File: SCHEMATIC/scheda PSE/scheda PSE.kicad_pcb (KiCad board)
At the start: 2 copper layers, 102.4 x 77.4 mm, 148 parts, among them J1 Conn_01x03, J2 Vin, J3 USB_B_Mini, J4 Vout 5V, J5 I2C_3V3, J6 UART0_3V3, Q1 IRLML0060TRPBF, Q2 PDTC114YT, Q3 IRLML9301, SW1 RESET_SW, SW2 PROG_SW, SW3 SW_U, SW4 SW_L, SW5 SW_R, SW6 SW_D, SW7 Power_button, U1 RP2040, U2 W25Q16JVUSSQ, U3 AT24C256, U4 oled_0.96"_128x64px, U5 TPS563201, U6 XC6705A331MR-G, U7 SAM-M8Q, U8 MMA8451Q, U9 TC1047A, Y1 12MHz

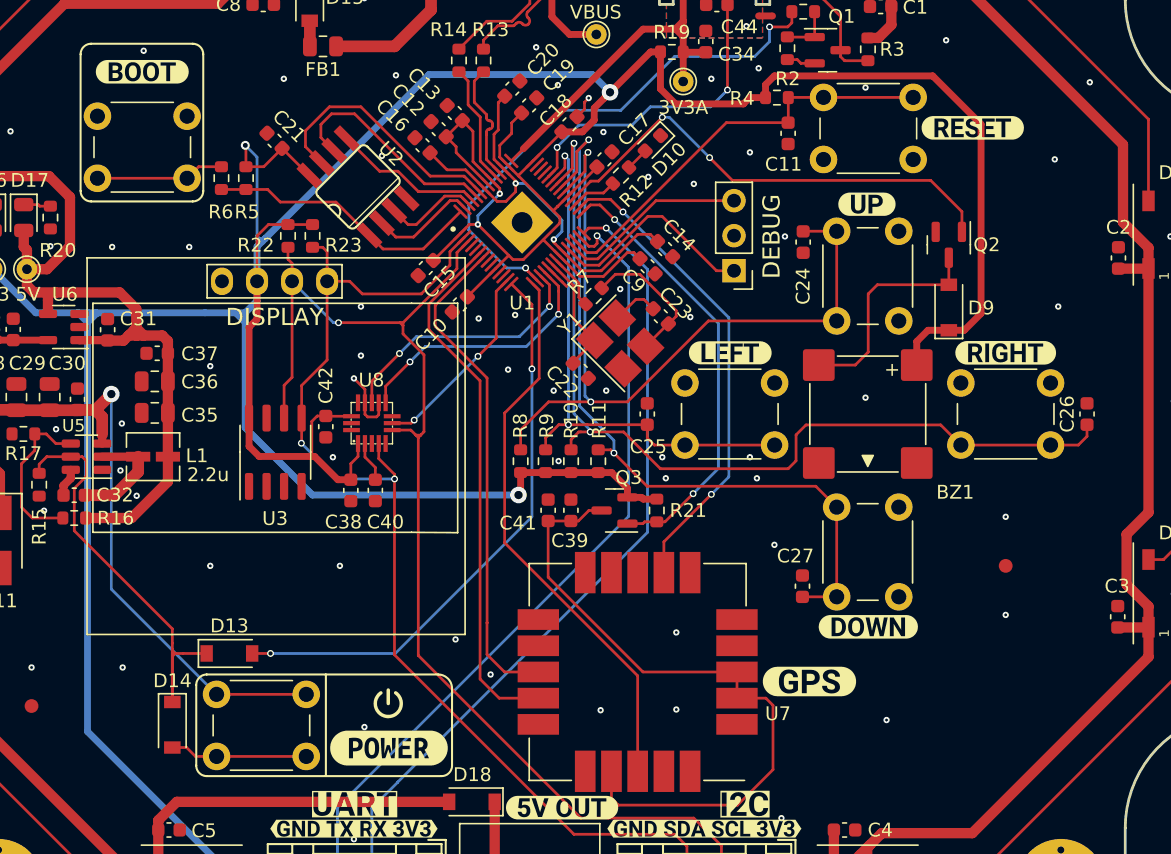
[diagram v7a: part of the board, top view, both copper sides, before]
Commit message: cambiati i pulsanti in smd
se servono gli altri pulsanti usare la versione precedente
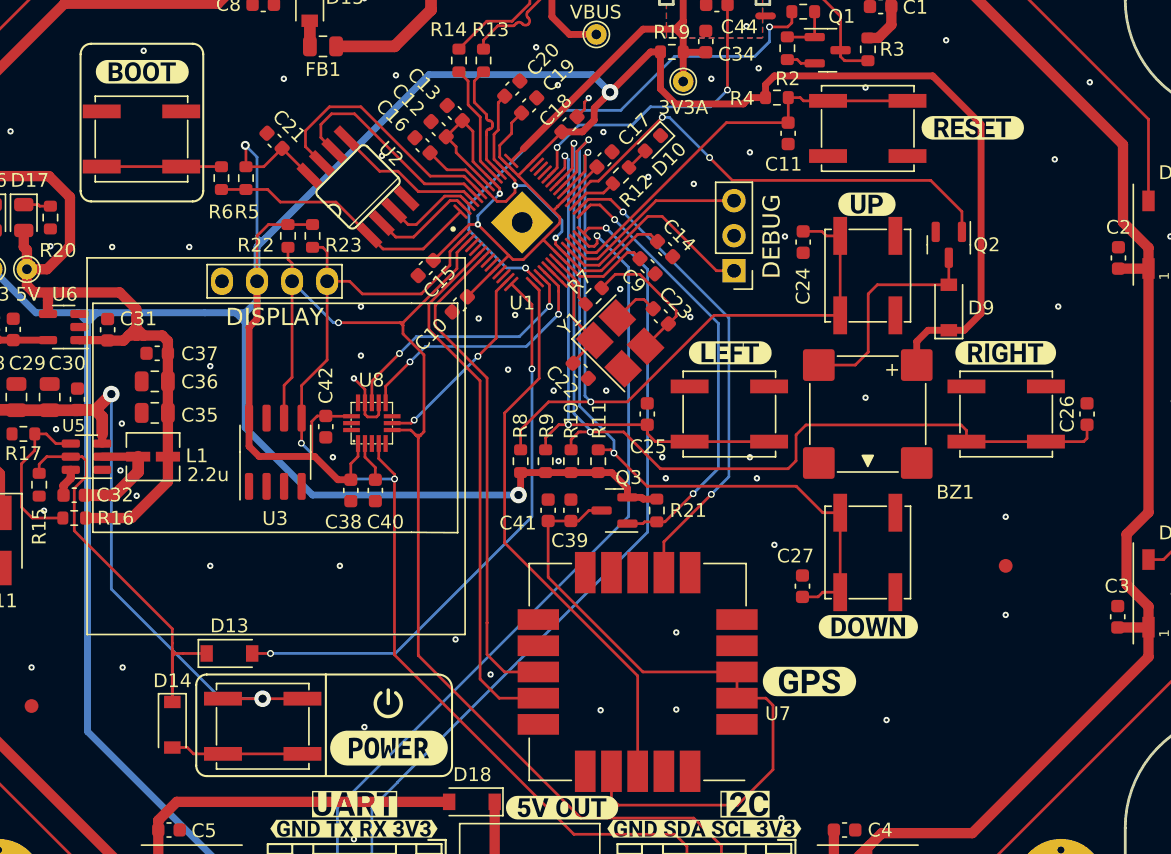
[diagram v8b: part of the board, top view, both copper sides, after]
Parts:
- SW1, SW2, SW3, SW4, SW5, SW6, SW7: footprint Button_Switch_THT:SW_PUSH_6mm_H5mm -> Button_Switch_SMD:SW_SPST_EVQP0
- moved SW2 4.36 mm to (127.4, 77.1)
- moved SW7 4.07 mm to (136.1, 119.6)
- moved SW1 3.99 mm to (180.0, 76.3)
- moved SW5 3.98 mm to (190.0, 97.0)
- moved SW4 3.93 mm to (170.0, 97.0)
- moved SW6 3.93 mm to (180.0, 107.0)
- moved SW3 3.93 mm to (180.0, 87.0)
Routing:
- net +12V: track 44.6 -> 47.4 mm, vias 1 -> 2
- net /Interfaccia utente/BUTTON_L: track 40.8 -> 40.1 mm
- net /RP2040/~{USB_BOOT}: track 9.33 -> 8.68 mm
